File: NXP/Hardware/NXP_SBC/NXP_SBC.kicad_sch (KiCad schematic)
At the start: 0 parts

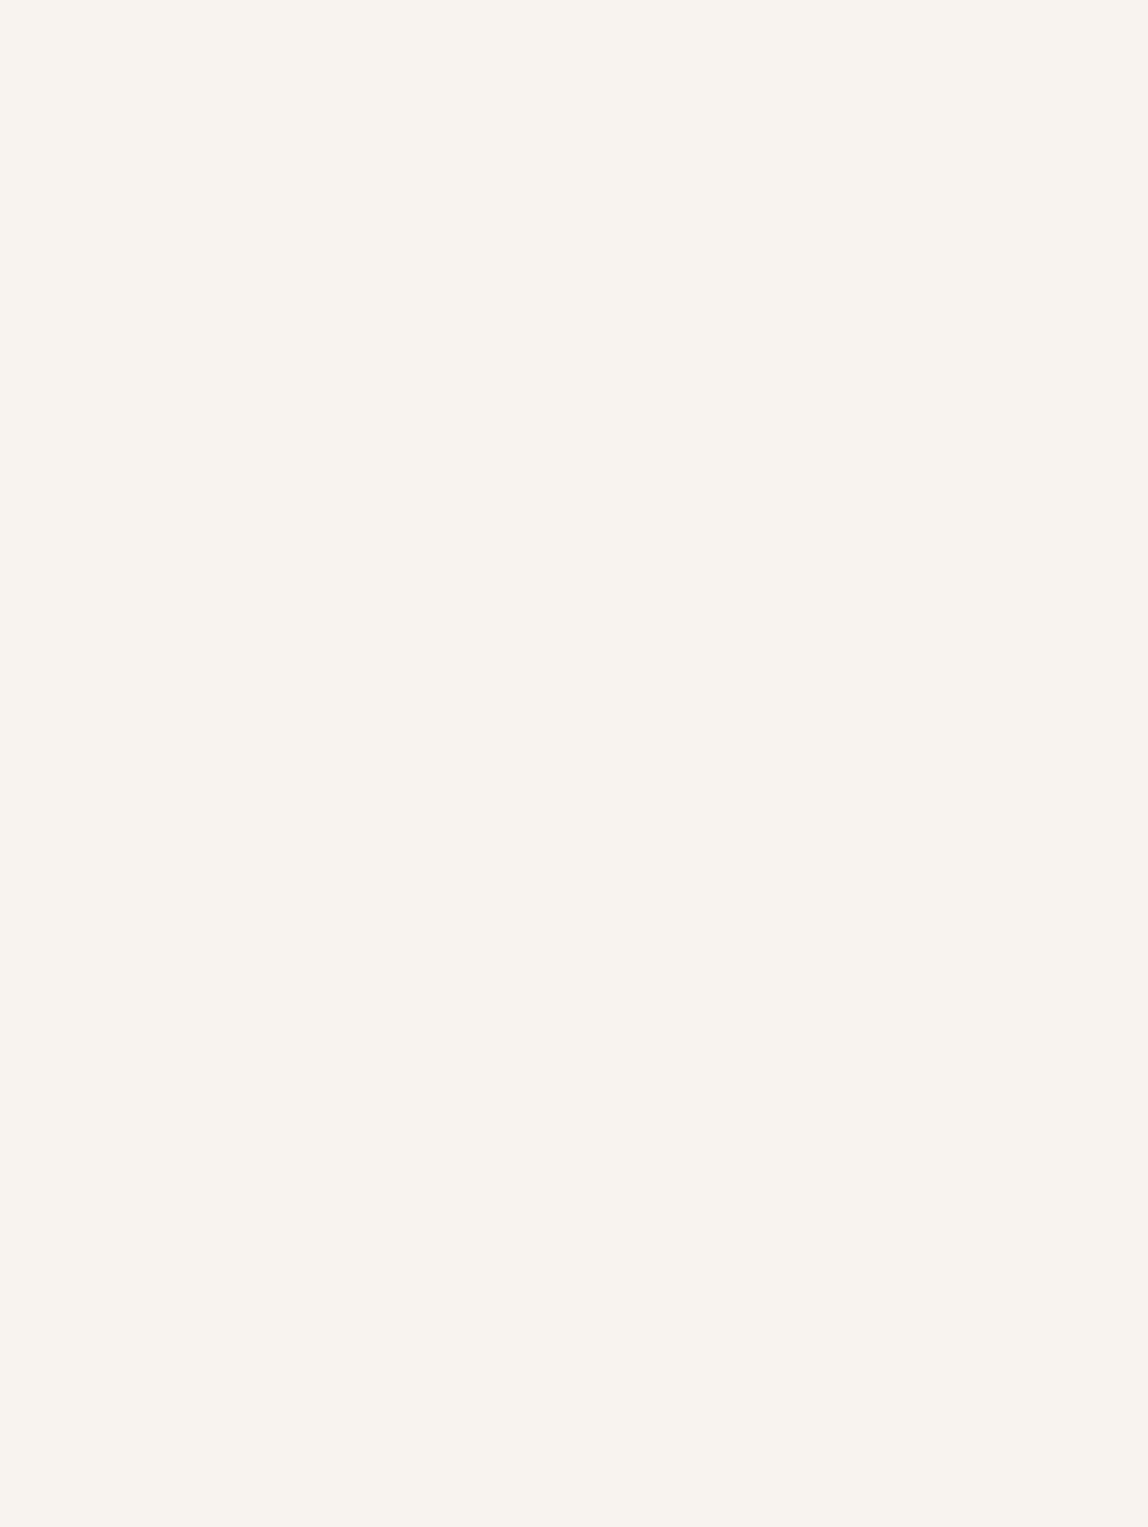
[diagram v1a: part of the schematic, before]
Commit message: Added more to ethernet schematic
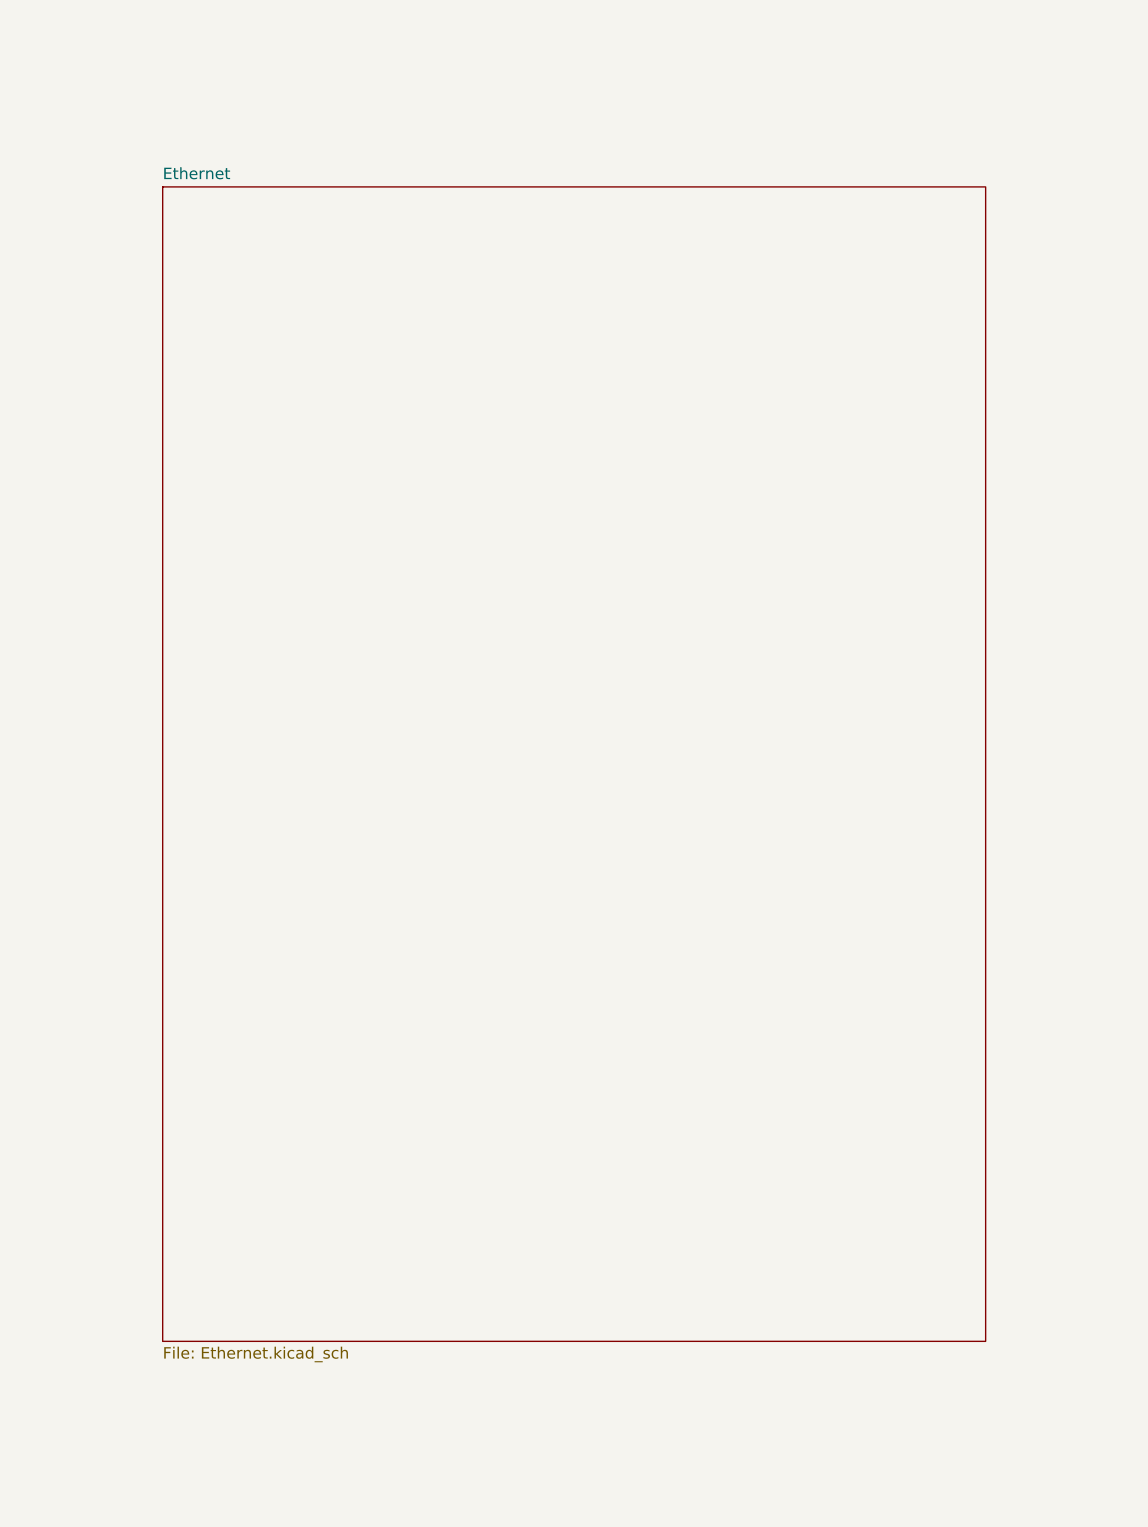
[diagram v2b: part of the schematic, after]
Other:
- added sheet Ethernet (Ethernet.kicad_sch)
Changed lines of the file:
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@@
 	(paper "A1")
+	(sheet
+		(at 322.58 105.41)
+		(size 91.44 128.27)
+		(exclude_from_sim no)
+		(in_bom yes)
+		(on_board yes)
+		(dnp no)
+		(fields_autoplaced yes)
+		(stroke
+			(width 0.1524)
+			(type solid)
+		)
+		(fill
+			(color 0 0 0 0.0000)
+		)
+		(property "Sheetname" "Ethernet"
+			(at 322.58 104.6984 0)
+			(effects
+				(font
+					(size 1.27 1.27)
+				)
+				(justify left bottom)
+			)
+		)
+		(property "Sheetfile" "Ethernet.kicad_sch"
+			(at 322.58 234.2646 0)
+			(effects
+				(font
+					(size 1.27 1.27)
+				)
+				(justify left top)
+			)
+		)
+		(instances
+			(project "NXP_SBC"
+				(path "/e82fc437-413b-4185-b609-66f66e24e498"
+					(page "6")
+				)
+			)
+		)
+	)
 	(sheet
 		(at 604.52 88.9)

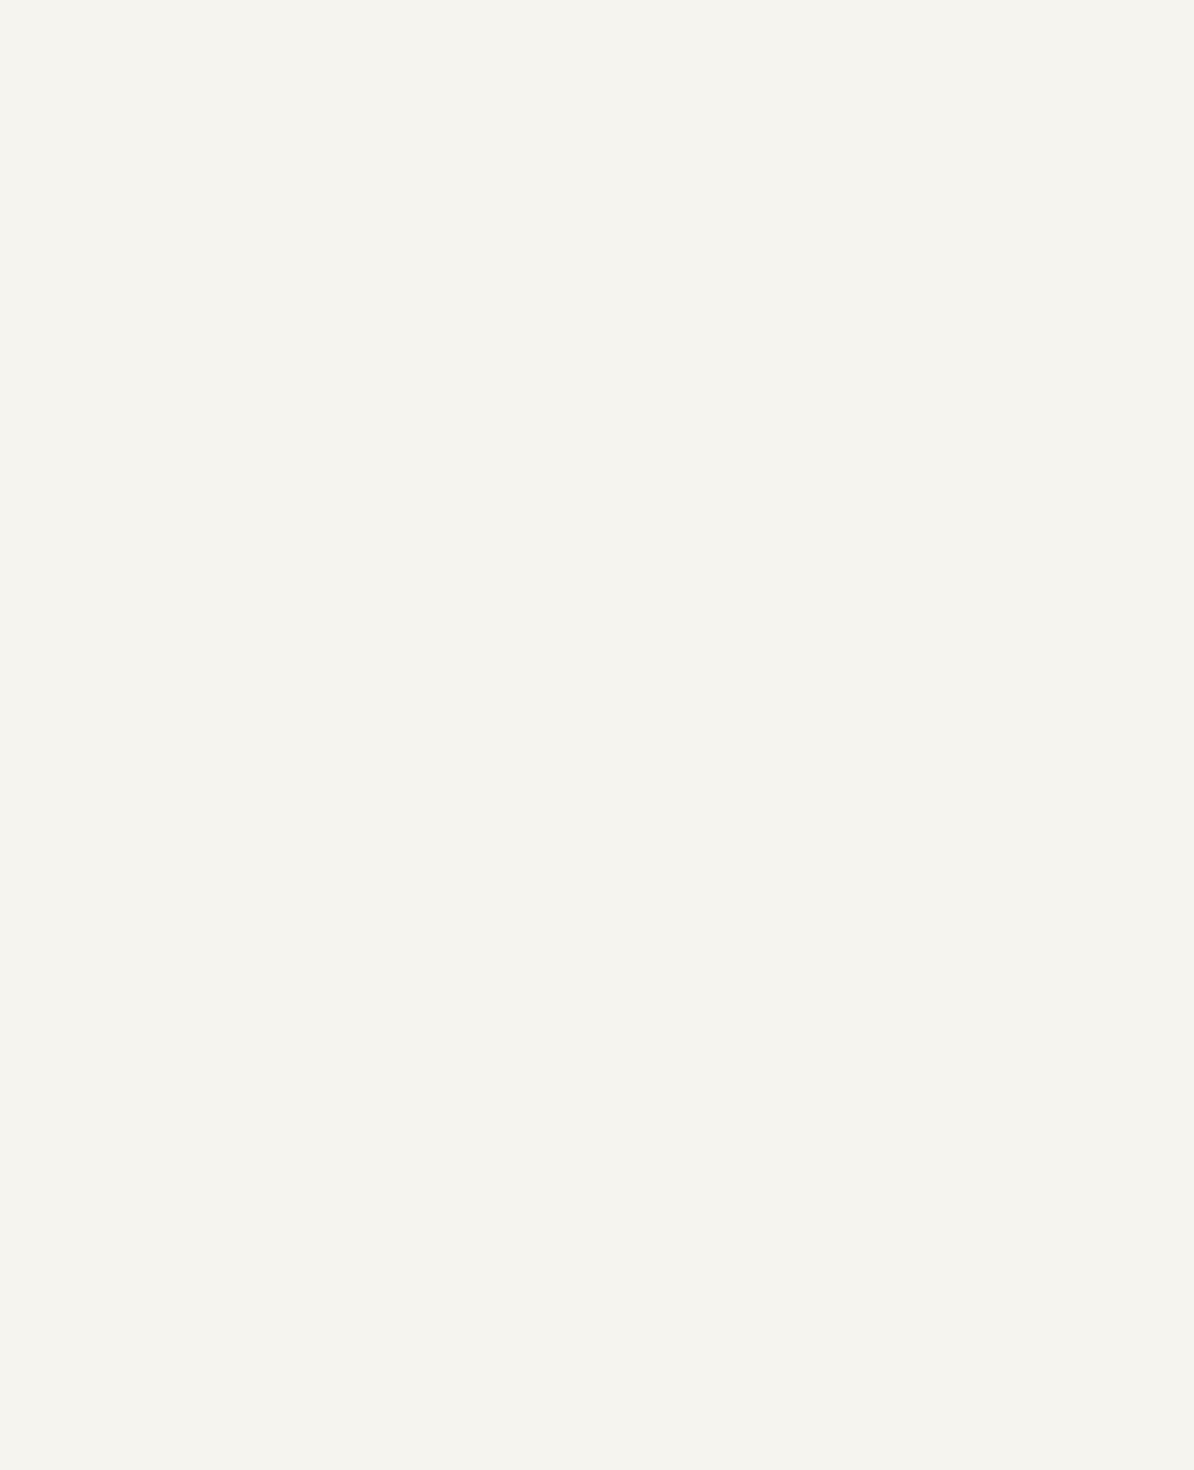
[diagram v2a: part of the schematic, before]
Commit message: added in Maya Wifi/BT module
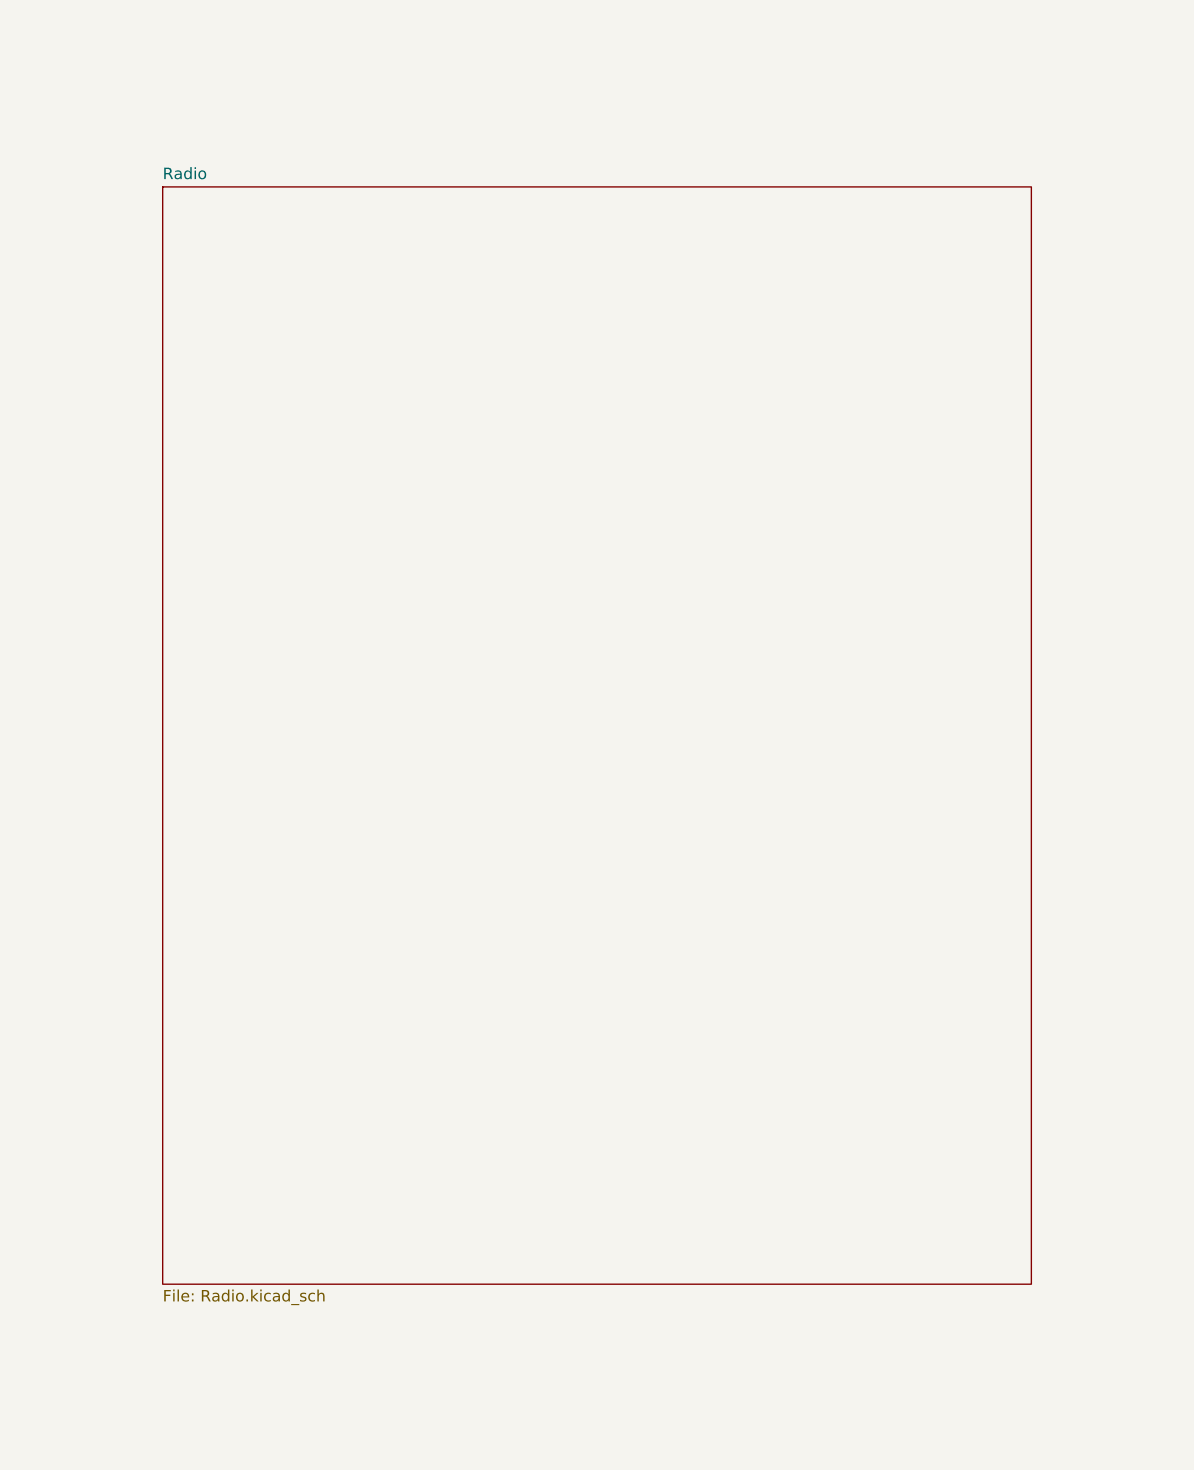
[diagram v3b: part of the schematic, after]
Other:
- added sheet Radio (Radio.kicad_sch)
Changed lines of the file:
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@@
+	)
+	(sheet
+		(at 431.8 304.8)
+		(size 96.52 121.92)
+		(exclude_from_sim no)
+		(in_bom yes)
+		(on_board yes)
+		(dnp no)
+		(fields_autoplaced yes)
+		(stroke
+			(width 0.1524)
+			(type solid)
+		)
+		(fill
+			(color 0 0 0 0.0000)
+		)
+		(property "Sheetname" "Radio"
+			(at 431.8 304.0884 0)
+			(effects
+				(font
+					(size 1.27 1.27)
+				)
+				(justify left bottom)
+			)
+		)
+		(property "Sheetfile" "Radio.kicad_sch"
+			(at 431.8 427.3046 0)
+			(effects
+				(font
+					(size 1.27 1.27)
+				)
+				(justify left top)
+			)
+		)
+		(instances
+			(project "NXP_SBC"
+				(path "/e82fc437-413b-4185-b609-66f66e24e498"
+					(page "7")
+				)
+			)
+		)
 	)
 	(sheet

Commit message: More additions to schematic
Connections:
- no-connect marks 0 -> 4
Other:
- sheet Ethernet ports: added ETH_CLK, ETH_CRS_DV, ETH_INT, ETH_MDC, ETH_MDIO, ETH_RXD0, ETH_RXD1, ETH_RXER, ETH_TXD0, ETH_TXD1, ETH_TXEN, ETH_nRST; removed none
- sheet Memory ports: added DDR_VREF, RAM_ADDR0, RAM_ADDR1, RAM_ADDR10, RAM_ADDR11, RAM_ADDR12, RAM_ADDR13, RAM_ADDR14, RAM_ADDR2, RAM_ADDR3, RAM_ADDR4, RAM_ADDR5, RAM_ADDR6, RAM_ADDR7, RAM_ADDR8, RAM_ADDR9, RAM_BANK_ADDR0, RAM_BANK_ADDR1, RAM_BANK_ADDR2, RAM_CAS#, RAM_CK, RAM_CK#, RAM_CKE, RAM_CS#, RAM_DQ0, RAM_DQ1, RAM_DQ10, RAM_DQ11, RAM_DQ12, RAM_DQ13, RAM_DQ14, RAM_DQ15, RAM_DQ2, RAM_DQ3, RAM_DQ4, RAM_DQ5, RAM_DQ6, RAM_DQ7, RAM_DQ8, RAM_DQ9, RAM_LDM, RAM_LDQS, RAM_LDQS#, RAM_ODT, RAM_RAS#, RAM_RESET, RAM_UDM, RAM_UDQS, RAM_UDQS#, RAM_WE#; removed none
- sheet Processor ports: added DRAM_ADDR00, DRAM_ADDR01, DRAM_ADDR02, DRAM_ADDR03, DRAM_ADDR04, DRAM_ADDR05, DRAM_ADDR06, DRAM_ADDR07, DRAM_ADDR08, DRAM_ADDR09, DRAM_ADDR10, DRAM_ADDR11, DRAM_ADDR12, DRAM_ADDR13, DRAM_ADDR14, DRAM_ADDR15, DRAM_CAS_B, DRAM_CS0_B, DRAM_CS1_B, DRAM_DATA0, DRAM_DATA1, DRAM_DATA10, DRAM_DATA11, DRAM_DATA12, DRAM_DATA13, DRAM_DATA14, DRAM_DATA15, DRAM_DATA2, DRAM_DATA3, DRAM_DATA4, DRAM_DATA5, DRAM_DATA6, DRAM_DATA7, DRAM_DATA8, DRAM_DATA9, DRAM_DQM0, DRAM_DQM1, DRAM_ODT0, DRAM_ODT1, DRAM_RAS_B, DRAM_SDBA0, DRAM_SDBA1, DRAM_SDBA2, DRAM_SDCLK0_N, DRAM_SDCLK0_P, DRAM_SDKE0, DRAM_SDKE1, DRAM_SDQS0_P, DRAM_SDQS1_N, DRAM_SDQS1_P, DRAM_SDQSO_N, DRAM_SDWE_B, DRAM_VREF, LCD_CLK, LCD_DATA00, LCD_DATA01, LCD_DATA02, LCD_DATA03, LCD_DATA04, LCD_DATA05, LCD_DATA06, LCD_DATA07, LCD_DATA08, LCD_DATA09, LCD_DATA10, LCD_DATA11, LCD_DATA12, LCD_DATA13, LCD_DATA14, LCD_DATA15, LCD_DATA16, LCD_DATA17, LCD_DATA18, LCD_DATA19, LCD_DATA20, LCD_DATA21, LCD_DATA22, LCD_DATA23, LCD_ENABLE, LCD_HSYNC, LCD_RESET, LCD_VSYNC, uP_ENET1_RX_DATA0, uP_ENET1_RX_DATA1, uP_ENET1_RX_EN, uP_ENET1_RX_ER, uP_ENET1_TX_CLK, uP_ENET1_TX_DATA0, uP_ENET1_TX_DATA1, uP_ENET1_TX_EN, uP_ENET1_nINT, uP_ENET2_RX_DATA0, uP_ENET2_RX_DATA1, uP_ENET2_RX_EN, uP_ENET2_RX_ER, uP_ENET2_TX_CLK, uP_ENET2_TX_DATA0, uP_ENET2_TX_DATA1, uP_ENET2_TX_EN, uP_ENET_MDC, uP_ENET_MDIO; removed none

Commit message: WIP
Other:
- sheet Memory ports: added SD_CLK, SD_CMD, SD_D0, SD_D1, SD_D2, SD_D3, SD_DET; removed none
- sheet Processor ports: added DRAM_RESET, uP_SD1_CLK, uP_SD1_CMD, uP_SD1_DATA0, uP_SD1_DATA1, uP_SD1_DATA2, uP_SD1_DATA3; removed uP_ENET2_RX_DATA0

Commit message: More updates to schematic
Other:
- sheet Connectors ports: added LCD_B0, LCD_B1, LCD_B2, LCD_B3, LCD_B4, LCD_B5, LCD_B6, LCD_B7, LCD_BIST, LCD_CLK, LCD_DEN, LCD_DISP, LCD_G0, LCD_G1, LCD_G2, LCD_G3, LCD_G4, LCD_G5, LCD_G6, LCD_G7, LCD_HSYNC, LCD_R0, LCD_R1, LCD_R2, LCD_R3, LCD_R4, LCD_R5, LCD_R6, LCD_R7, LCD_VSYNC, TS_INT, TS_RESET, TS_SCL, TS_SDA, USB_D+, USB_D-; removed none
- sheet Processor ports: added uP_I2C_SCL, uP_I2C_SDA; removed none

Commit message: WIP
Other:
- sheet Connectors ports: added none; removed LCD_BIST
- sheet Processor ports: added uP_LCD_DISP, uP_TS_INT, uP_TS_RESET, uP_USB_OTG1_DN, uP_USB_OTG1_DP; removed none
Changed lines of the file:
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@@
+	(wire
+		(pts
+			(xy 495.3 140.97) (xy 511.81 140.97)
+		)
+		(stroke
+			(width 0)
+			(type default)
+		)
+	)
 	(wire
 		(pts
@@
 	(wire
 		(pts
+			(xy 495.3 260.35) (xy 511.81 260.35)
+		)
+		(stroke
+			(width 0)
+			(type default)
+		)
+	)
+	(wire
+		(pts
 			(xy 495.3 201.93) (xy 511.81 201.93)
 		)
@@
 	(wire
 		(pts
+			(xy 495.3 228.6) (xy 511.81 228.6)
+		)
+		(stroke
+			(width 0)
+			(type default)
+		)
+	)
+	(wire
+		(pts
 			(xy 495.3 181.61) (xy 511.81 181.61)
 		)
@@
 	(wire
 		(pts
+			(xy 495.3 236.22) (xy 511.81 236.22)
+		)
+		(stroke
+			(width 0)
+			(type default)
+		)
+	)
+	(wire
+		(pts
 			(xy 495.3 209.55) (xy 511.81 209.55)
 		)
@@
 		(pts
 			(xy 355.6 261.62) (xy 386.08 261.62)
+		)
+		(stroke
+			(width 0)
+			(type default)
+		)
+	)
+	(wire
+		(pts
+			(xy 495.3 257.81) (xy 511.81 257.81)
 		)
 		(stroke
@@
 		)
 		(pin "LCD_RESET" input
-			(at 495.3 138.43 0)
+			(at 472.44 135.89 90)
 			(effects
 				(font
@@
 		(pin "uP_I2C_SDA" input
 			(at 495.3 233.68 0)
+			(effects
+				(font
+					(size 1.27 1.27)
+				)
+				(justify right)
+			)
+		)
+		(pin "uP_USB_OTG1_DN" input
+			(at 495.3 260.35 0)
+			(effects
+				(font
+					(size 1.27 1.27)
+				)
+				(justify right)
+			)
+		)
+		(pin "uP_USB_OTG1_DP" input
+			(at 495.3 257.81 0)
+			(effects
+				(font
+					(size 1.27 1.27)
+				)
+				(justify right)
+			)
+		)
+		(pin "uP_LCD_DISP" input
+			(at 495.3 140.97 0)
+			(effects
+				(font
+					(size 1.27 1.27)
+				)
+				(justify right)
+			)
+		)
+		(pin "uP_TS_INT" input
+			(at 495.3 228.6 0)
+			(effects
+				(font
+					(size 1.27 1.27)
+				)
+				(justify right)
+			)
+		)
+		(pin "uP_TS_RESET" input
+			(at 495.3 236.22 0)
 			(effects
 				(font
@@
 			)
 		)
-		(pin "LCD_BIST" input
-			(at 511.81 154.94 180)
-			(effects
-				(font
-					(size 1.27 1.27)
-				)
-				(justify left)
-			)
-		)
 		(pin "LCD_CLK" input
 			(at 511.81 151.13 180)
@@
 		)
 		(pin "LCD_DISP" input
-			(at 511.81 138.43 180)
-			(effects
-				(font
+			(at 511.81 140.97 180)
+			(effects
+				(font
